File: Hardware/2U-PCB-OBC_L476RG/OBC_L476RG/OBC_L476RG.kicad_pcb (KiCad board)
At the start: 2 copper layers, 90 x 92 mm, 7 parts, among them J1 Bus Standard, J2 Micro_SD_Card_Det_Hirose_DM3AT, U2 NUCLEO_L476RG

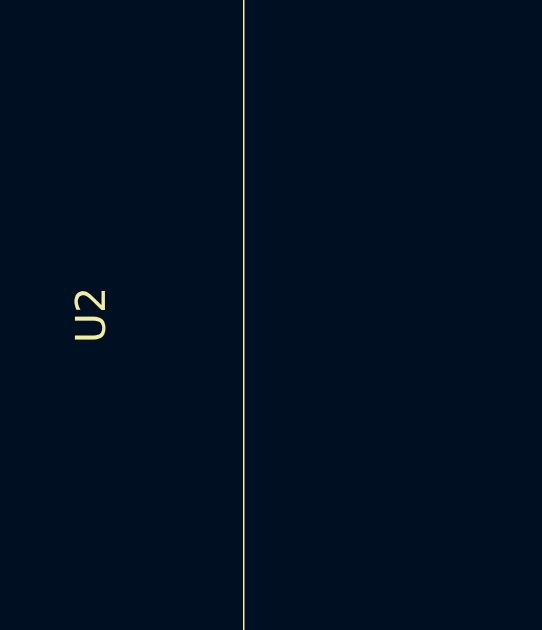
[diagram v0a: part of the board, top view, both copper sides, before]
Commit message: Some libraries were added for NAND gate. Also I2C in mikrobus changed. ROuting started respecting constraints.
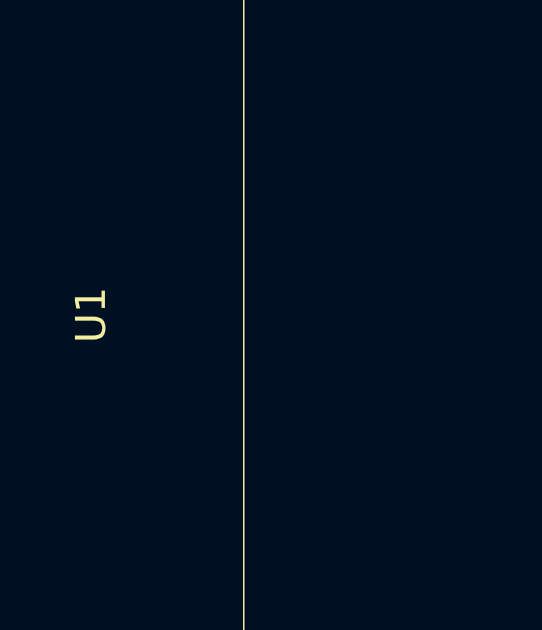
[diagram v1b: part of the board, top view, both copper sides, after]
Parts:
- B1: value ~ -> Buffer
- renumbered U2 to U1
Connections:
- U1 pad 18: +5V -> unconnected-(U1-+5V-Pad18)
